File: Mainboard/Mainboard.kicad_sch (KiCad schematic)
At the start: 27 parts, among them J1 Bus_M.2_Socket_E, J3 USB_A_Stacked, J4 Micro_SD_Card, J6 Conn_01x09_Pin, J7 Conn_01x09_Pin, U1 Hirose DF40C-100DS-0.4V, U2 ADS1115IDGS, U3 PCM5102, U4 PAM8403D

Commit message: New larger layout size (PCB)
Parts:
- J1: footprint M.2_2230_E:2230-key-E -> Connector_PCBEdge:M.2_2230-xx-E
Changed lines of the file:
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@@
 			)
 		)
-		(property "Footprint" "M.2_2230_E:2230-key-E"
+		(property "Footprint" "Connector_PCBEdge:M.2_2230-xx-E"
 			(at 331.47 111.76 0)
 			(hide yes)

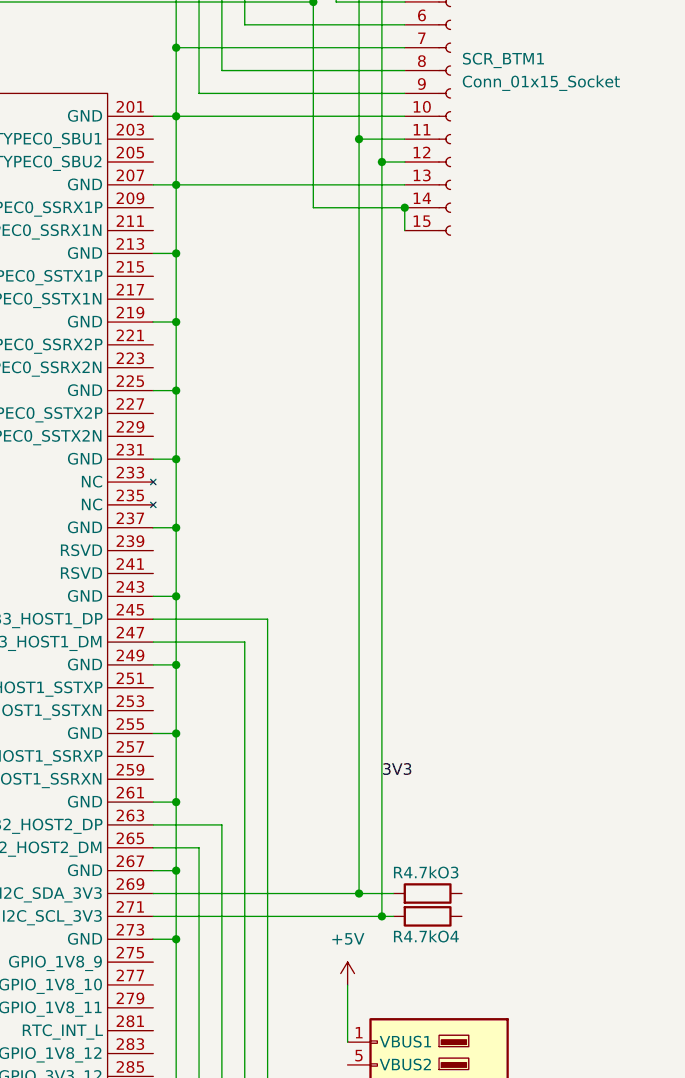
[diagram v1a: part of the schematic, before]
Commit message: Fixed M.2 Connector Setup
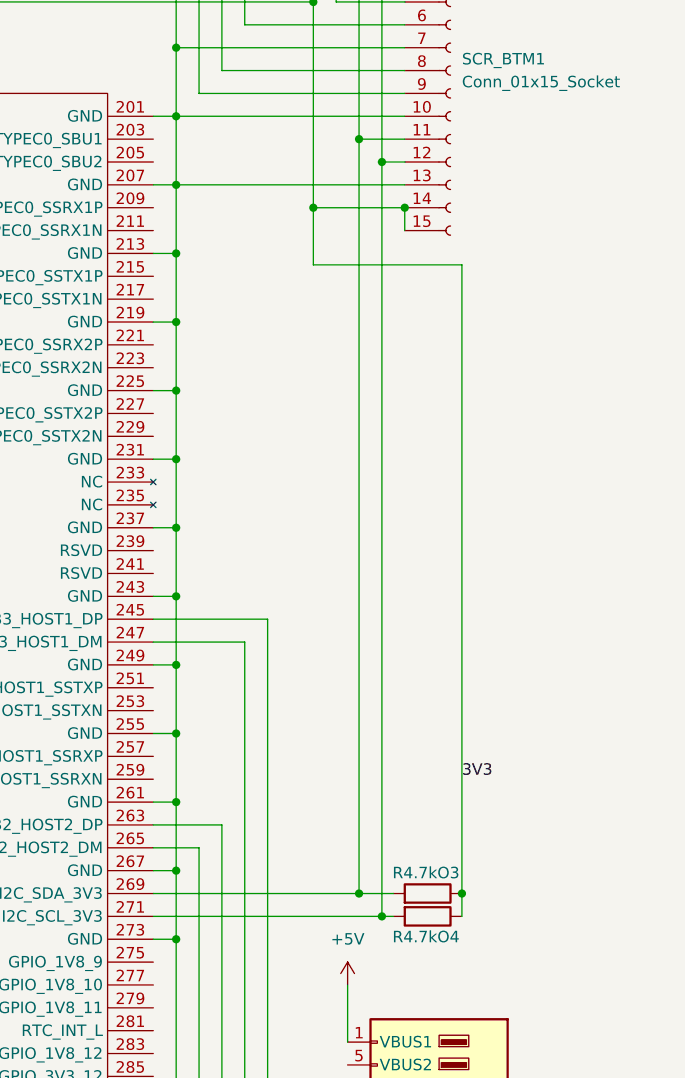
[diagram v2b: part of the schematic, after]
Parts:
- J1: footprint Connector_PCBEdge:M.2_2230-xx-E -> 2199230-8:TE_2199230-8
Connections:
- net 3V3: now also R4.7kO3.1, R4.7kO4.1; no longer R4.7kO4.2, SCR_BTM1.12 (Pin_12), SCR_TOP1.12 (Pin_12), U1.271 (I2C_SCL_3V3)
- new net: R4.7kO4.2, SCR_BTM1.12 (Pin_12), SCR_TOP1.12 (Pin_12), U1.271 (I2C_SCL_3V3)
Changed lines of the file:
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@@
 	)
 	(junction
+		(at 469.9 330.2)
+		(diameter 0)
+		(color 0 0 0 0)
+	)
+	(junction
+		(at 453.39 254)
+		(diameter 0)
+		(color 0 0 0 0)
+	)
+	(junction
 		(at 113.03 146.05)
 		(diameter 0)
@@
 	(wire
 		(pts
+			(xy 469.9 260.35) (xy 469.9 330.2)
+		)
+		(stroke
+			(width 0)
+			(type default)
+		)
+	)
+	(wire
+		(pts
 			(xy 81.28 129.54) (xy 78.74 129.54)
 		)
@@
 	(wire
 		(pts
+			(xy 469.9 260.35) (xy 453.39 260.35)
+		)
+		(stroke
+			(width 0)
+			(type default)
+		)
+	)
+	(wire
+		(pts
 			(xy 189.23 181.61) (xy 205.74 181.61)
 		)
@@
 	(wire
 		(pts
+			(xy 453.39 260.35) (xy 453.39 254)
+		)
+		(stroke
+			(width 0)
+			(type default)
+		)
+	)
+	(wire
+		(pts
 			(xy 204.47 171.45) (xy 204.47 189.23)
 		)
@@
 	(wire
 		(pts
-			(xy 461.01 332.74) (xy 461.01 248.92)
+			(xy 461.01 248.92) (xy 461.01 332.74)
 		)
 		(stroke
@@
 	(wire
 		(pts
+			(xy 469.9 332.74) (xy 469.9 330.2)
+		)
+		(stroke
+			(width 0)
+			(type default)
+		)
+	)
+	(wire
+		(pts
 			(xy 135.89 172.72) (xy 146.05 172.72)
 		)
@@
 	)
 	(label "3V3"
-		(at 461.01 317.5 0)
+		(at 469.9 317.5 0)
 		(effects
 			(font
@@
 			)
 		)
-		(property "Footprint" "Connector_PCBEdge:M.2_2230-xx-E"
+		(property "Footprint" "2199230-8:TE_2199230-8"
 			(at 331.47 111.76 0)
 			(hide yes)

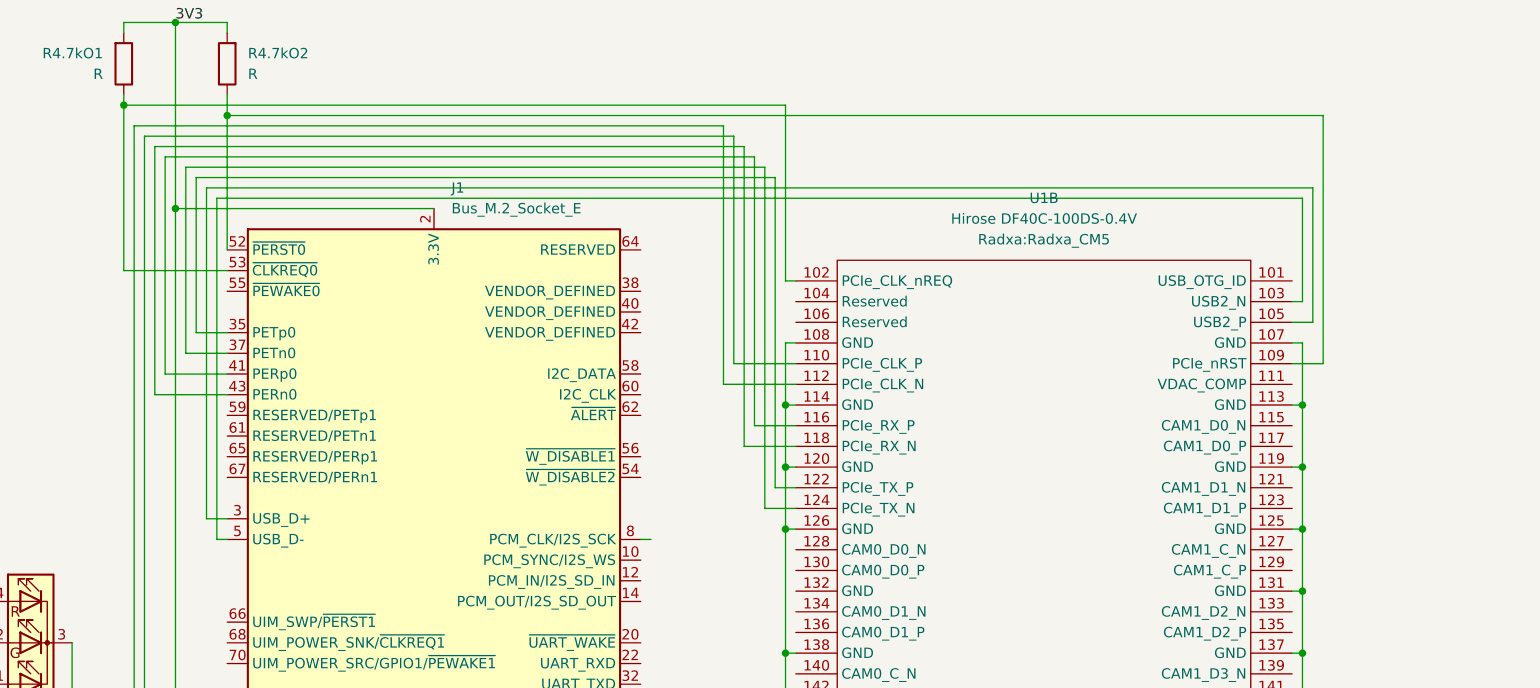
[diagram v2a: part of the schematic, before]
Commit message: Routed Wifi; USB_D, TX and RX Dfpairs
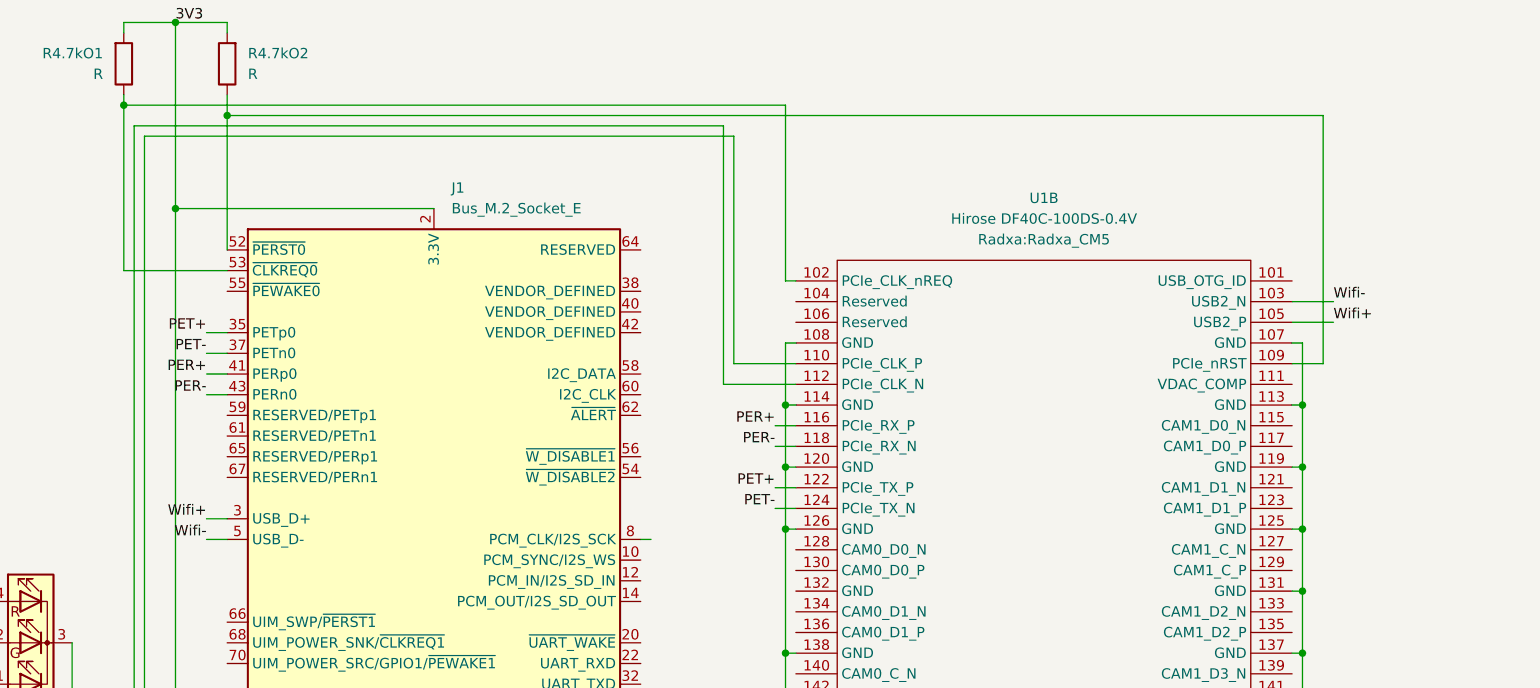
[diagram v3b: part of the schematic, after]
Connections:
- net Wifi-: now reaches J1.5 (USB_D-), U1.103 (USB2_N)
- net Wifi+: now reaches J1.3 (USB_D+), U1.105 (USB2_P)
- net PER+: now reaches J1.41 (PERp0), U1.116 (PCIe_RX_P)
- net PER-: now reaches J1.43 (PERn0), U1.118 (PCIe_RX_N)
- net PET+: now reaches J1.35 (PETp0), U1.122 (PCIe_TX_P)
- net PET-: now reaches J1.37 (PETn0), U1.124 (PCIe_TX_N)

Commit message: Wifi Card Connected!
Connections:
- net RFCLK+: now reaches J1.47 (REFCLKp0), U1.110 (PCIe_CLK_P)
- net RFCLK-: now reaches J1.49 (REFCLKn0), U1.112 (PCIe_CLK_N)
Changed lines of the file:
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@@
 	(wire
 		(pts
-			(xy 375.92 109.22) (xy 368.3 109.22)
-		)
-		(stroke
-			(width 0)
-			(type default)
-		)
-	)
-	(wire
-		(pts
 			(xy 435.61 312.42) (xy 438.15 312.42)
 		)
@@
 	(wire
 		(pts
-			(xy 295.91 81.28) (xy 295.91 173.99)
-		)
-		(stroke
-			(width 0)
-			(type default)
-		)
-	)
-	(wire
-		(pts
 			(xy 463.55 226.06) (xy 448.31 226.06)
 		)
@@
 	(wire
 		(pts
+			(xy 373.38 109.22) (xy 375.92 109.22)
+		)
+		(stroke
+			(width 0)
+			(type default)
+		)
+	)
+	(wire
+		(pts
 			(xy 200.66 231.14) (xy 200.66 243.84)
 		)
@@
 	(wire
 		(pts
+			(xy 303.53 176.53) (xy 306.07 176.53)
+		)
+		(stroke
+			(width 0)
+			(type default)
+		)
+	)
+	(wire
+		(pts
 			(xy 135.89 199.39) (xy 146.05 199.39)
 		)
@@
 	(wire
 		(pts
-			(xy 165.1 125.73) (xy 205.74 125.73)
+			(xy 373.38 111.76) (xy 375.92 111.76)
 		)
 		(stroke
@@
 	(wire
 		(pts
-			(xy 295.91 173.99) (xy 306.07 173.99)
+			(xy 165.1 125.73) (xy 205.74 125.73)
 		)
 		(stroke
@@
 	(wire
 		(pts
-			(xy 294.64 80.01) (xy 294.64 176.53)
-		)
-		(stroke
-			(width 0)
-			(type default)
-		)
-	)
-	(wire
-		(pts
 			(xy 455.93 208.28) (xy 455.93 231.14)
 		)
@@
 	(wire
 		(pts
-			(xy 368.3 109.22) (xy 368.3 81.28)
-		)
-		(stroke
-			(width 0)
-			(type default)
-		)
-	)
-	(wire
-		(pts
 			(xy 266.7 107.95) (xy 267.97 107.95)
 		)
@@
 	(wire
 		(pts
-			(xy 294.64 176.53) (xy 306.07 176.53)
-		)
-		(stroke
-			(width 0)
-			(type default)
-		)
-	)
-	(wire
-		(pts
 			(xy 266.7 186.69) (xy 266.7 189.23)
 		)
@@
 	(wire
 		(pts
+			(xy 303.53 173.99) (xy 306.07 173.99)
+		)
+		(stroke
+			(width 0)
+			(type default)
+		)
+	)
+	(wire
+		(pts
 			(xy 368.3 81.28) (xy 295.91 81.28)
 		)
@@
 	(wire
 		(pts
-			(xy 375.92 111.76) (xy 367.03 111.76)
-		)
-		(stroke
-			(width 0)
-			(type default)
-		)
-	)
-	(wire
-		(pts
 			(xy 146.05 199.39) (xy 146.05 201.93)
 		)
@@
 	(wire
 		(pts
-			(xy 367.03 111.76) (xy 367.03 80.01)
-		)
-		(stroke
-			(width 0)
-			(type default)
-		)
-	)
-	(wire
-		(pts
 			(xy 130.81 107.95) (xy 97.79 107.95)
 		)
@@
 		)
 	)
+	(label "RFCLK-"
+		(at 303.53 176.53 180)
+		(effects
+			(font
+				(size 1.27 1.27)
+			)
+			(justify right bottom)
+		)
+	)
 	(label "Wifi+"
 		(at 441.96 104.14 0)
@@
 		)
 	)
+	(label "RFCLK+"
+		(at 373.38 109.22 180)
+		(effects
+			(font
+				(size 1.27 1.27)
+			)
+			(justify right bottom)
+		)
+	)
 	(label "PET+"
 		(at 303.53 105.41 180)
@@
 		)
 	)
+	(label "RFCLK+"
+		(at 303.53 173.99 180)
+		(effects
+			(font
+				(size 1.27 1.27)
+			)
+			(justify right bottom)
+		)
+	)
 	(label "Wifi-"
 		(at 303.53 130.81 180)
@@
 		)
 	)
+	(label "RFCLK-"
+		(at 373.38 111.76 180)
+		(effects
+			(font
+				(size 1.27 1.27)
+			)
+			(justify right bottom)
+		)
+	)

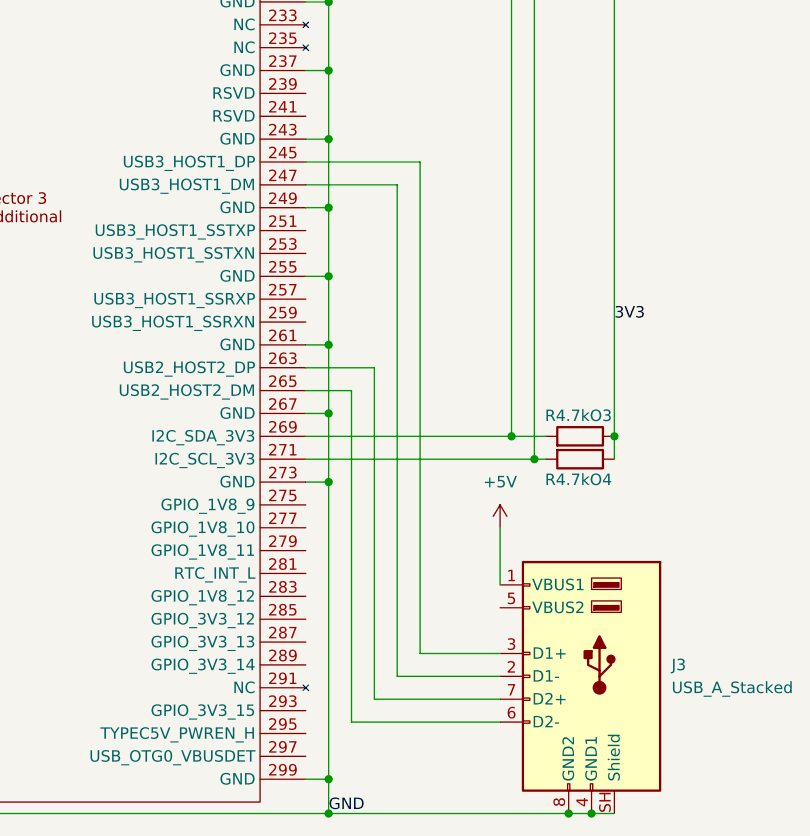
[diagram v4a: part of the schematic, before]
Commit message: Half Routed USB Tower
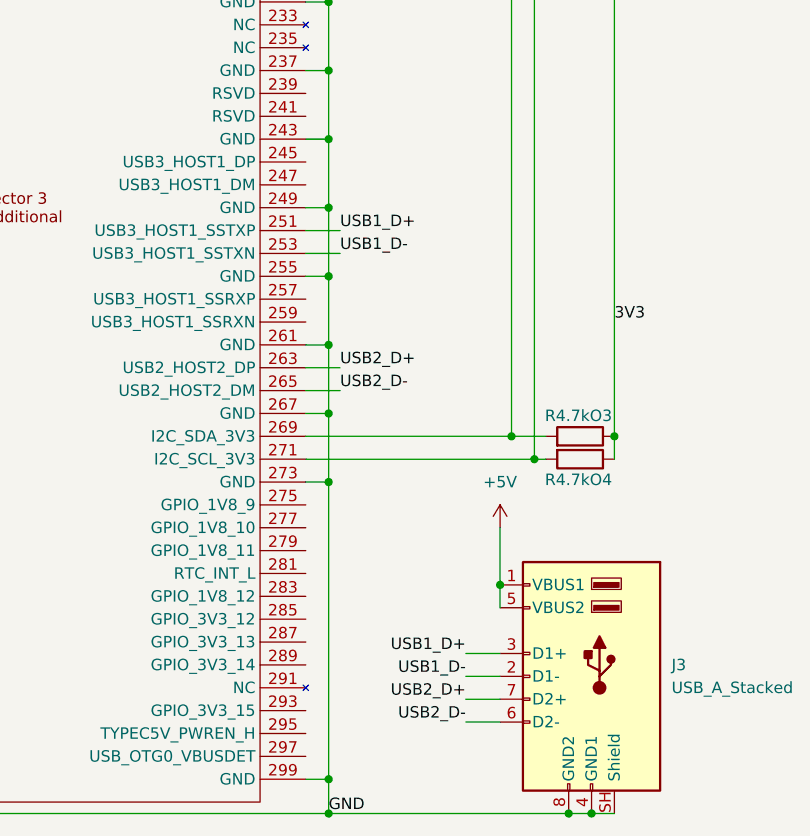
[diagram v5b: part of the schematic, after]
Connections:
- net +5V: now also J3.5 (VBUS2)
- net at U1.245 (USB3_HOST1_DP): no longer J3.3 (D1+)
- net at U1.247 (USB3_HOST1_DM): no longer J3.2 (D1-)
- net USB1_D+: now reaches U1.251 (USB3_HOST1_SSTXP)
- net USB1_D+: now also J3.3 (D1+)
- net USB1_D-: now reaches U1.253 (USB3_HOST1_SSTXN)
- net USB1_D-: now also J3.2 (D1-)
- net USB2_D+: now reaches J3.7 (D2+), U1.263 (USB2_HOST2_DP)
- net USB2_D-: now reaches J3.6 (D2-), U1.265 (USB2_HOST2_DM)
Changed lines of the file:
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@@
 	)
 	(junction
+		(at 457.2 346.71)
+		(diameter 0)
+		(color 0 0 0 0)
+	)
+	(junction
 		(at 374.65 228.6)
 		(diameter 0)
@@
 	(wire
 		(pts
-			(xy 445.77 356.87) (xy 445.77 302.26)
-		)
-		(stroke
-			(width 0)
-			(type default)
-		)
-	)
-	(wire
-		(pts
 			(xy 274.32 138.43) (xy 276.86 138.43)
 		)
@@
 	(wire
 		(pts
-			(xy 443.23 359.41) (xy 457.2 359.41)
-		)
-		(stroke
-			(width 0)
-			(type default)
-		)
-	)
-	(wire
-		(pts
 			(xy 205.74 135.89) (xy 161.29 135.89)
 		)
@@
 	(wire
 		(pts
-			(xy 204.47 147.32) (xy 204.47 153.67)
+			(xy 457.2 354.33) (xy 453.39 354.33)
 		)
 		(stroke
@@
 	(wire
 		(pts
-			(xy 95.25 147.32) (xy 95.25 143.51)
+			(xy 204.47 147.32) (xy 204.47 153.67)
 		)
 		(stroke
@@
 	(wire
 		(pts
-			(xy 448.31 354.33) (xy 448.31 299.72)
+			(xy 95.25 147.32) (xy 95.25 143.51)
 		)
 		(stroke
@@
 	(wire
 		(pts
-			(xy 457.2 356.87) (xy 445.77 356.87)
-		)
-		(stroke
-			(width 0)
-			(type default)
-		)
-	)
-	(wire
-		(pts
 			(xy 156.21 110.49) (xy 156.21 165.1)
 		)
@@
 	(wire
 		(pts
+			(xy 457.2 346.71) (xy 457.2 349.25)
+		)
+		(stroke
+			(width 0)
+			(type default)
+		)
+	)
+	(wire
+		(pts
 			(xy 438.15 243.84) (xy 435.61 243.84)
 		)
@@
 	(wire
 		(pts
+			(xy 435.61 322.58) (xy 439.42 322.58)
+		)
+		(stroke
+			(width 0)
+			(type default)
+		)
+	)
+	(wire
+		(pts
 			(xy 374.65 175.26) (xy 374.65 182.88)
 		)
@@
 	(wire
 		(pts
+			(xy 435.61 307.34) (xy 439.42 307.34)
+		)
+		(stroke
+			(width 0)
+			(type default)
+		)
+	)
+	(wire
+		(pts
 			(xy 148.59 200.66) (xy 189.23 200.66)
 		)
@@
 	(wire
 		(pts
-			(xy 440.69 325.12) (xy 440.69 361.95)
-		)
-		(stroke
-			(width 0)
-			(type default)
-		)
-	)
-	(wire
-		(pts
 			(xy 267.97 107.95) (xy 267.97 95.25)
 		)
@@
 	(wire
 		(pts
-			(xy 443.23 322.58) (xy 443.23 359.41)
-		)
-		(stroke
-			(width 0)
-			(type default)
-		)
-	)
-	(wire
-		(pts
 			(xy 306.07 95.25) (xy 306.07 78.74)
 		)
@@
 	(wire
 		(pts
-			(xy 435.61 302.26) (xy 445.77 302.26)
-		)
-		(stroke
-			(width 0)
-			(type default)
-		)
-	)
-	(wire
-		(pts
 			(xy 113.03 146.05) (xy 97.79 146.05)
 		)
@@
 	(wire
 		(pts
-			(xy 435.61 325.12) (xy 440.69 325.12)
-		)
-		(stroke
-			(width 0)
-			(type default)
-		)
-	)
-	(wire
-		(pts
 			(xy 461.01 248.92) (xy 461.01 332.74)
 		)
@@
 	(wire
 		(pts
+			(xy 457.2 361.95) (xy 453.39 361.95)
+		)
+		(stroke
+			(width 0)
+			(type default)
+		)
+	)
+	(wire
+		(pts
 			(xy 266.7 181.61) (xy 266.7 184.15)
 		)
@@
 	(wire
 		(pts
-			(xy 457.2 354.33) (xy 448.31 354.33)
+			(xy 457.2 356.87) (xy 453.39 356.87)
 		)
 		(stroke
@@
 	(wire
 		(pts
-			(xy 440.69 361.95) (xy 457.2 361.95)
-		)
-		(stroke
-			(width 0)
-			(type default)
-		)
-	)
-	(wire
-		(pts
 			(xy 204.47 161.29) (xy 205.74 161.29)
 		)
@@
 	(wire
 		(pts
+			(xy 457.2 359.41) (xy 453.39 359.41)
+		)
+		(stroke
+			(width 0)
+			(type default)
+		)
+	)
+	(wire
+		(pts
 			(xy 463.55 195.58) (xy 453.39 195.58)
 		)
@@
 	(wire
 		(pts
-			(xy 435.61 322.58) (xy 443.23 322.58)
-		)
-		(stroke
-			(width 0)
-			(type default)
-		)
-	)
-	(wire
-		(pts
 			(xy 267.97 76.2) (xy 267.97 80.01)
 		)
@@
 	(wire
 		(pts
+			(xy 435.61 309.88) (xy 439.42 309.88)
+		)
+		(stroke
+			(width 0)
+			(type default)
+		)
+	)
+	(wire
+		(pts
 			(xy 204.47 130.81) (xy 204.47 143.51)
 		)
@@
 	(wire
 		(pts
-			(xy 435.61 299.72) (xy 448.31 299.72)
+			(xy 331.47 90.17) (xy 299.72 90.17)
 		)
 		(stroke
@@
 	(wire
 		(pts
-			(xy 331.47 90.17) (xy 299.72 90.17)
+			(xy 374.65 77.47) (xy 374.65 99.06)
 		)
 		(stroke
@@
 	(wire
 		(pts
-			(xy 374.65 77.47) (xy 374.65 99.06)
+			(xy 435.61 325.12) (xy 439.42 325.12)
 		)
 		(stroke
@@
 		)
 	)
+	(label "USB2_D-"
+		(at 439.42 325.12 0)
+		(effects
+			(font
+				(size 1.27 1.27)
+			)
+			(justify left bottom)
+		)
+	)
 	(label "PER+"
 		(at 373.38 116.84 180)
@@
 		)
 	)
+	(label "USB1_D+"
+		(at 439.42 307.34 0)
+		(effects
+			(font
+				(size 1.27 1.27)
+			)
+			(justify left bottom)
+		)
+	)
 	(label "PET-"
 		(at 303.53 107.95 180)
@@
 		)
 	)
+	(label "USB1_D+"
+		(at 453.39 354.33 180)
+		(effects
+			(font
+				(size 1.27 1.27)
+			)
+			(justify right bottom)
+		)
+	)
 	(label "3V3"
 		(at 469.9 317.5 0)
@@
 		)
 	)
+	(label "USB2_D+"
+		(at 439.42 322.58 0)
+		(effects
+			(font
+				(size 1.27 1.27)
+			)
+			(justify left bottom)
+		)
+	)
 	(label "LED_WIFI1 => G+B"
 		(at 354.33 208.28 0)
@@
 		)
 	)
+	(label "USB2_D+"
+		(at 453.39 359.41 180)
+		(effects
+			(font
+				(size 1.27 1.27)
+			)
+			(justify right bottom)
+		)
+	)
 	(label "Wifi-"
 		(at 303.53 130.81 180)
@@
 		)
 	)
+	(label "USB1_D-"
+		(at 439.42 309.88 0)
+		(effects
+			(font
+				(size 1.27 1.27)
+			)
+			(justify left bottom)
+		)
+	)
+	(label "USB1_D-"
+		(at 453.39 356.87 180)
+		(effects
+			(font
+				(size 1.27 1.27)
+			)
+			(justify right bottom)
+		)
+	)
 	(label "3V3"
 		(at 306.07 231.14 0)
@@
 		(effects
 			(font
+				(size 1.27 1.27)
+			)
+			(justify right bottom)
+		)
+	)
+	(label "USB2_D-"
+		(at 453.39 361.95 180)
+		(effects
+			(font
